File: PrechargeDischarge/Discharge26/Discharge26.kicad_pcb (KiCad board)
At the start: 2 copper layers, 80 x 105 mm, 11 parts, among them J1 HV_Conn, J2 LV_Conn, K4 Relay_SPST-NC, Q1 Q_NMOS_GSD

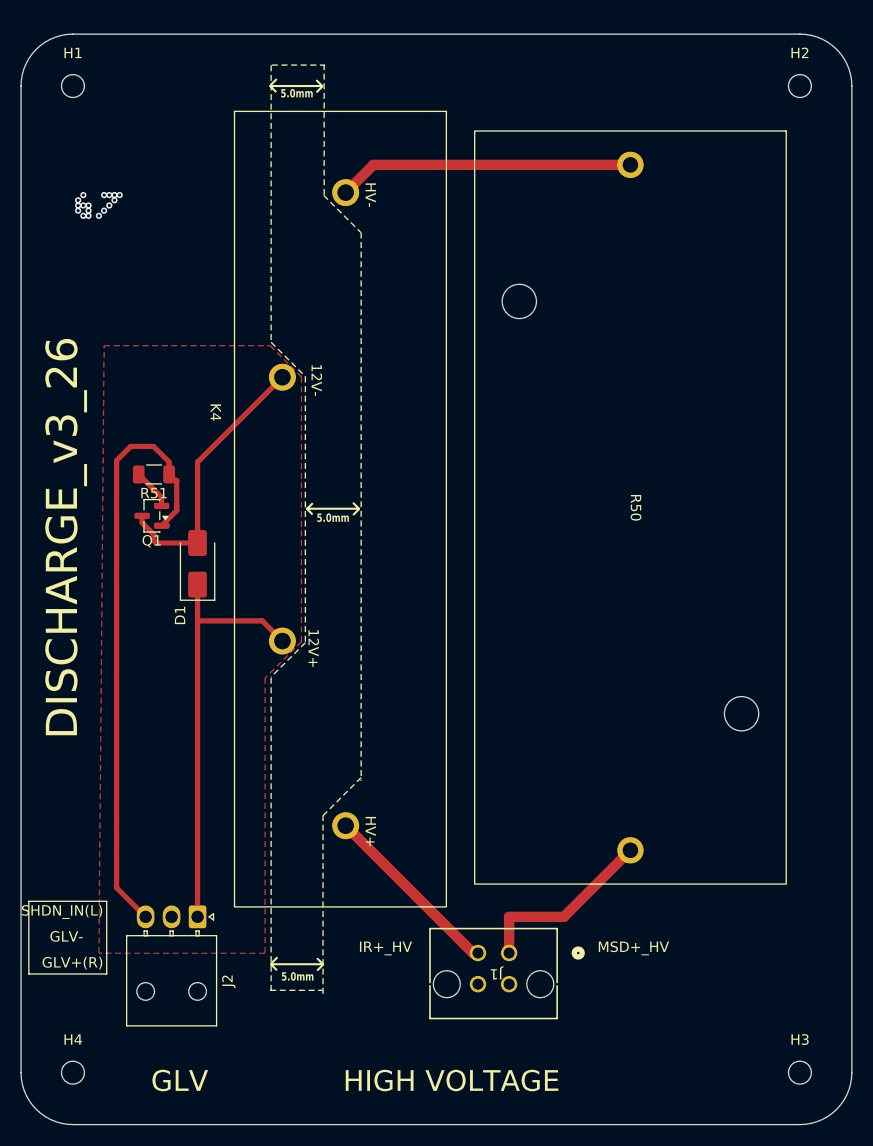
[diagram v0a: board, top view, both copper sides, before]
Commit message: changes mounting holes on discharge to M4
gareth wants all pcb mounting holes to M4
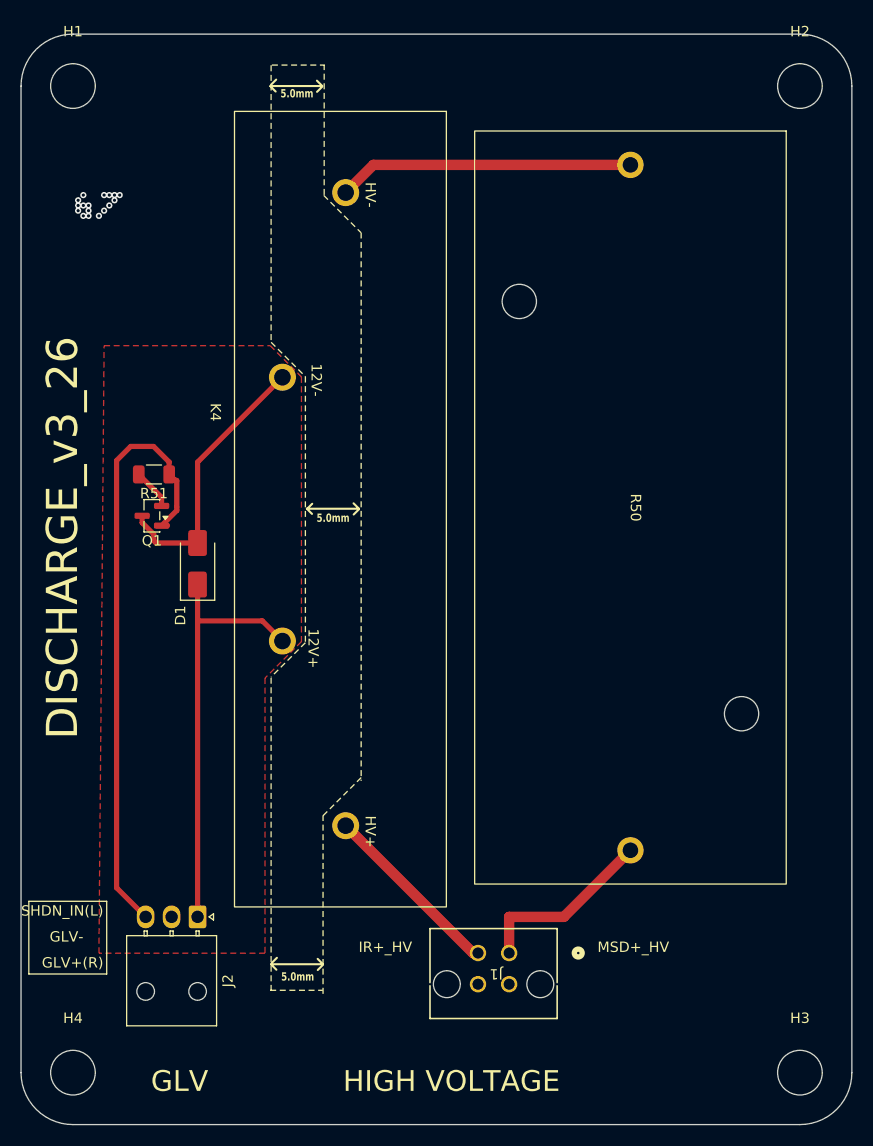
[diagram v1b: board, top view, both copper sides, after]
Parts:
- H1, H2, H3, H4: footprint MountingHole:MountingHole_2.2mm_M2 -> MountingHole:MountingHole_4.3mm_M4
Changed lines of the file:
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@@
 		)
 	)
-	(footprint "MountingHole:MountingHole_2.2mm_M2"
+	(footprint "MountingHole:MountingHole_4.3mm_M4"
 		(layer "F.Cu")
 		(at 130 140)
-		(descr "Mounting Hole 2.2mm, M2, no annular, generated by kicad-footprint-generator mountinghole.py")
-		(tags "mountinghole M2")
+		(descr "Mounting Hole 4.3mm, M4, no annular, generated by kicad-footprint-generator mountinghole.py")
+		(tags "mountinghole M4")
 		(property "Reference" "H4"
-			(at 0 -3.15 0)
+			(at 0 -5.25 0)
 			(layer "F.SilkS")
 			(effects
@@
 		)
 		(property "Value" "MountingHole"
-			(at 0 3.15 0)
+			(at 0 5.25 0)
 			(layer "F.Fab")
 			(effects
@@
 		(fp_circle
 			(center 0 0)
-			(end 2.2 0)
+			(end 4.3 0)
 			(stroke
 				(width 0.15)
@@
 		(fp_circle
 			(center 0 0)
-			(end 2.45 0)
+			(end 4.55 0)
 			(stroke
 				(width 0.05)
@@
 		(pad "" np_thru_hole circle
 			(at 0 0)
-			(size 2.2 2.2)
-			(drill 2.2)
+			(size 4.3 4.3)
+			(drill 4.3)
 			(layers "*.Cu" "*.Mask")
 		)
@@
 		)
 	)
-	(footprint "MountingHole:MountingHole_2.2mm_M2"
+	(footprint "MountingHole:MountingHole_4.3mm_M4"
 		(layer "F.Cu")
 		(at 130 45)
-		(descr "Mounting Hole 2.2mm, M2, no annular, generated by kicad-footprint-generator mountinghole.py")
-		(tags "mountinghole M2")
+		(descr "Mounting Hole 4.3mm, M4, no annular, generated by kicad-footprint-generator mountinghole.py")
+		(tags "mountinghole M4")
 		(property "Reference" "H1"
-			(at 0 -3.15 0)
+			(at 0 -5.25 0)
 			(layer "F.SilkS")
 			(effects
@@
 		)
 		(property "Value" "MountingHole"
-			(at 0 3.15 0)
+			(at 0 5.25 0)
 			(layer "F.Fab")
 			(effects
@@
 		(fp_circle
 			(center 0 0)
-			(end 2.2 0)
+			(end 4.3 0)
 			(stroke
 				(width 0.15)
@@
 		(fp_circle
 			(center 0 0)
-			(end 2.45 0)
+			(end 4.55 0)
 			(stroke
 				(width 0.05)
@@
 		(pad "" np_thru_hole circle
 			(at 0 0)
-			(size 2.2 2.2)
-			(drill 2.2)
+			(size 4.3 4.3)
+			(drill 4.3)
 			(layers "*.Cu" "*.Mask")
 		)
@@
 		(embedded_fonts no)
 	)
-	(footprint "MountingHole:MountingHole_2.2mm_M2"
+	(footprint "MountingHole:MountingHole_4.3mm_M4"
 		(layer "F.Cu")
 		(at 200 140)
-		(descr "Mounting Hole 2.2mm, M2, no annular, generated by kicad-footprint-generator mountinghole.py")
-		(tags "mountinghole M2")
+		(descr "Mounting Hole 4.3mm, M4, no annular, generated by kicad-footprint-generator mountinghole.py")
+		(tags "mountinghole M4")
 		(property "Reference" "H3"
-			(at 0 -3.15 0)
+			(at 0 -5.25 0)
 			(layer "F.SilkS")
 			(effects
@@
 		)
 		(property "Value" "MountingHole"
-			(at 0 3.15 0)
+			(at 0 5.25 0)
 			(layer "F.Fab")
 			(effects
@@
 		(fp_circle
 			(center 0 0)
-			(end 2.2 0)
+			(end 4.3 0)
 			(stroke
 				(width 0.15)
@@
 		(fp_circle
 			(center 0 0)
-			(end 2.45 0)
+			(end 4.55 0)
 			(stroke
 				(width 0.05)
@@
 		(pad "" np_thru_hole circle
 			(at 0 0)
-			(size 2.2 2.2)
-			(drill 2.2)
+			(size 4.3 4.3)
+			(drill 4.3)
 			(layers "*.Cu" "*.Mask")
 		)
@@
 		)
 	)
-	(footprint "MountingHole:MountingHole_2.2mm_M2"
+	(footprint "MountingHole:MountingHole_4.3mm_M4"
 		(layer "F.Cu")
 		(at 200 45)
-		(descr "Mounting Hole 2.2mm, M2, no annular, generated by kicad-footprint-generator mountinghole.py")
-		(tags "mountinghole M2")
+		(descr "Mounting Hole 4.3mm, M4, no annular, generated by kicad-footprint-generator mountinghole.py")
+		(tags "mountinghole M4")
 		(property "Reference" "H2"
-			(at 0 -3.15 0)
+			(at 0 -5.25 0)
 			(layer "F.SilkS")
 			(effects
@@
 		)
 		(property "Value" "MountingHole"
-			(at 0 3.15 0)
+			(at 0 5.25 0)
 			(layer "F.Fab")
 			(effects
@@
 		(fp_circle
 			(center 0 0)
-			(end 2.2 0)
+			(end 4.3 0)
 			(stroke
 				(width 0.15)
@@
 		(fp_circle
 			(center 0 0)
-			(end 2.45 0)
+			(end 4.55 0)
 			(stroke
 				(width 0.05)
@@
 		(pad "" np_thru_hole circle
 			(at 0 0)
-			(size 2.2 2.2)
-			(drill 2.2)
+			(size 4.3 4.3)
+			(drill 4.3)
 			(layers "*.Cu" "*.Mask")
 		)

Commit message: Discharge
Added through hole mosfets and LED driver to DIscharge board
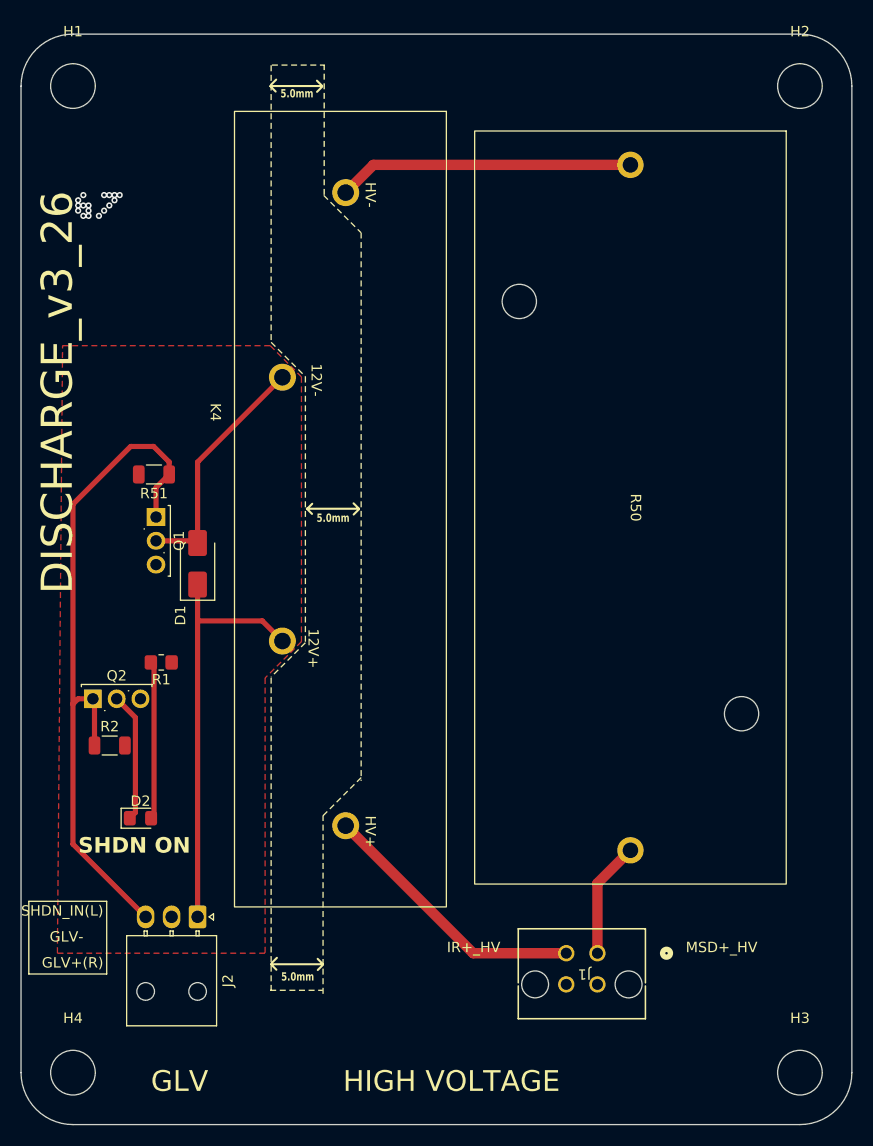
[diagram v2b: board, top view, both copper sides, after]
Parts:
- added D2: LED_DischargeOFF, LED_SMD:LED_0805_2012Metric_Pad1.15x1.40mm_HandSolder, F.Cu at (136.5, 115.5)
- added Q2: Q_NMOS_GDS, Package_TO_SOT_THT:TO-251-3_Vertical, F.Cu at (131.9, 104.0)
- added R1: 2k, Resistor_SMD:R_0805_2012Metric_Pad1.20x1.40mm_HandSolder, F.Cu at (138.5, 100.5)
- added R2: 10k, Resistor_SMD:R_1206_3216Metric, F.Cu at (133.5, 108.5)
- Q1: value Q_NMOS_GSD -> Q_NMOS_GDS; footprint Package_TO_SOT_SMD:SOT-23 -> Package_TO_SOT_THT:TO-251-3_Vertical
- moved J1 8.50 mm to (179.2, 130.0)
- moved Q1 0.42 mm to (138.0, 86.5), turned to -90 degrees
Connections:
- Q1 pad 2: GND -> Net-(D1-A)
- Q1 pad 3: Net-(D1-A) -> GND
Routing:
- net Net-(D2-A): track 0.00 -> 15.2 mm
- net Net-(D2-K): track 0.00 -> 12.5 mm
- net /IR+: track 17.8 -> 26.3 mm
- net /SHDN: track 59.0 -> 67.3 mm
- net /MSD_IN: track 17.8 -> 11.2 mm
- net GND: track 3.94 -> 0.00 mm
- net Net-(D1-A): track 26.5 -> 23.4 mm
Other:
- board text added: "SHDN ON"

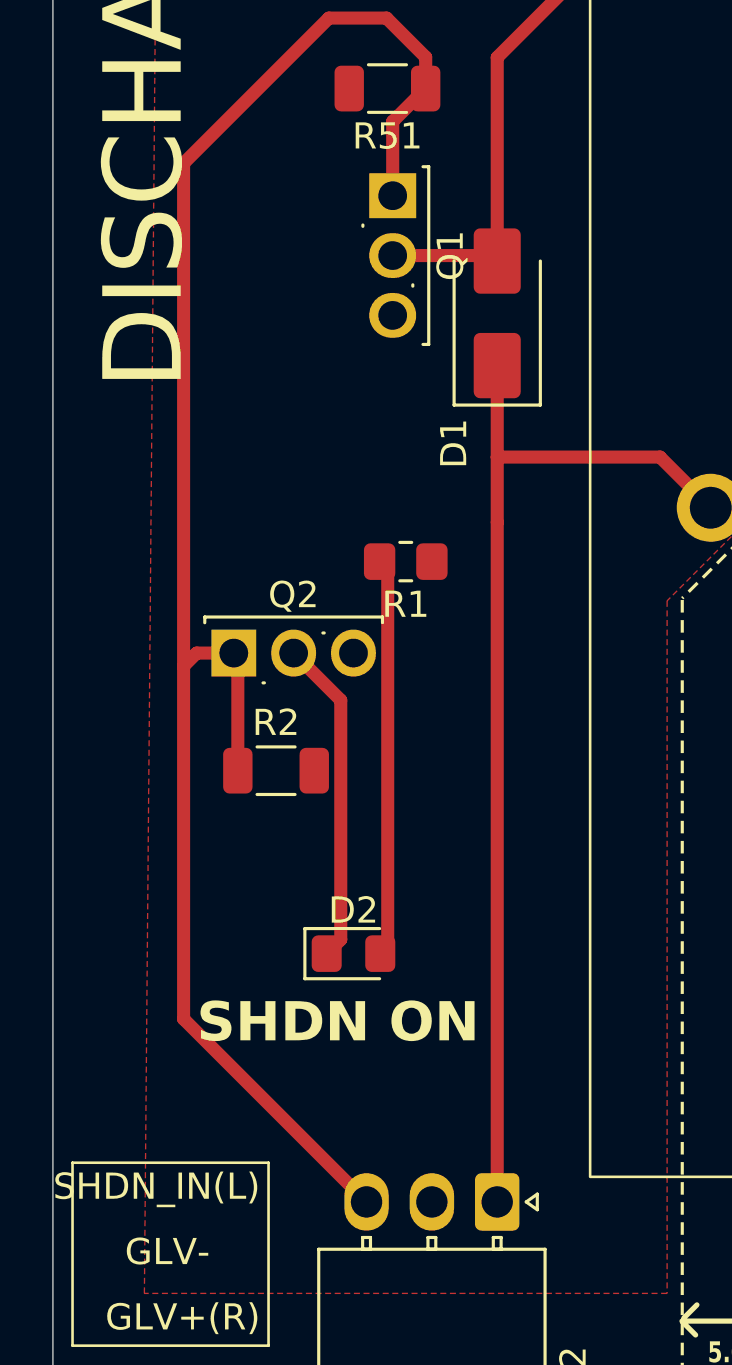
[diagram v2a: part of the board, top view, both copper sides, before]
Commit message: discharge fixed
added zener diode from nmos gate to source, also added indiactor LED
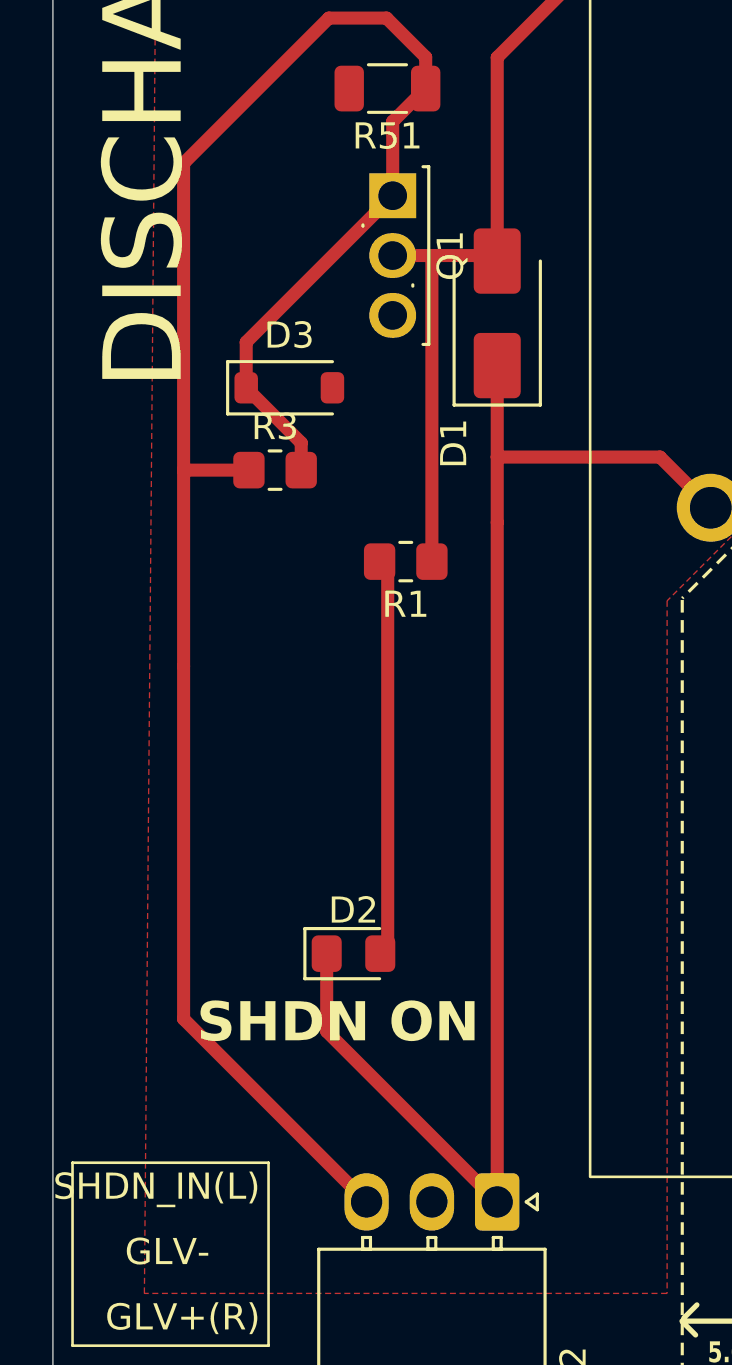
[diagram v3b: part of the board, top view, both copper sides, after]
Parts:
- removed Q2: Q_NMOS_GDS, Package_TO_SOT_THT:TO-251-3_Vertical
- removed R2: 10k, Resistor_SMD:R_1206_3216Metric
- added D3: D_Zener, Diode_SMD:D_SOD-123, F.Cu at (134.0, 93.8)
- added R3: 100, Resistor_SMD:R_0805_2012Metric_Pad1.20x1.40mm_HandSolder, F.Cu at (133.5, 97.0)
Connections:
- D2 pad 1: Net-(D2-K) -> +12V
- Q1 pad 1: /SHDN -> Net-(D3-K)
- R1 pad 1: +12V -> Net-(D1-A)
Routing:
- net Net-(D3-K): track 0.00 -> 13.0 mm
- net Net-(D2-K): track 12.5 -> 0.00 mm
- net +12V: track 41.0 -> 53.2 mm
- net Net-(D1-A): track 23.4 -> 35.1 mm
- net /SHDN: track 67.3 -> 63.1 mm

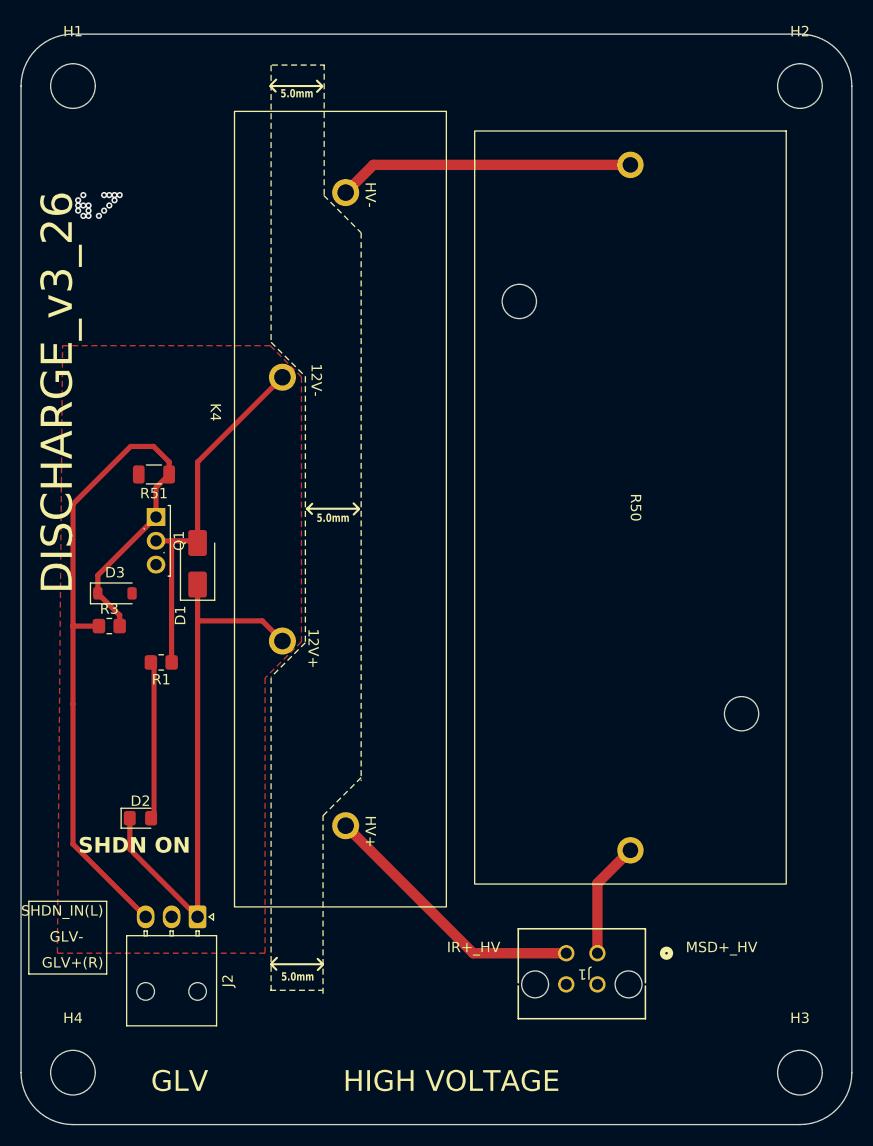
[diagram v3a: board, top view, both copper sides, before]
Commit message: Fixed Discharge + Added RML Quick files
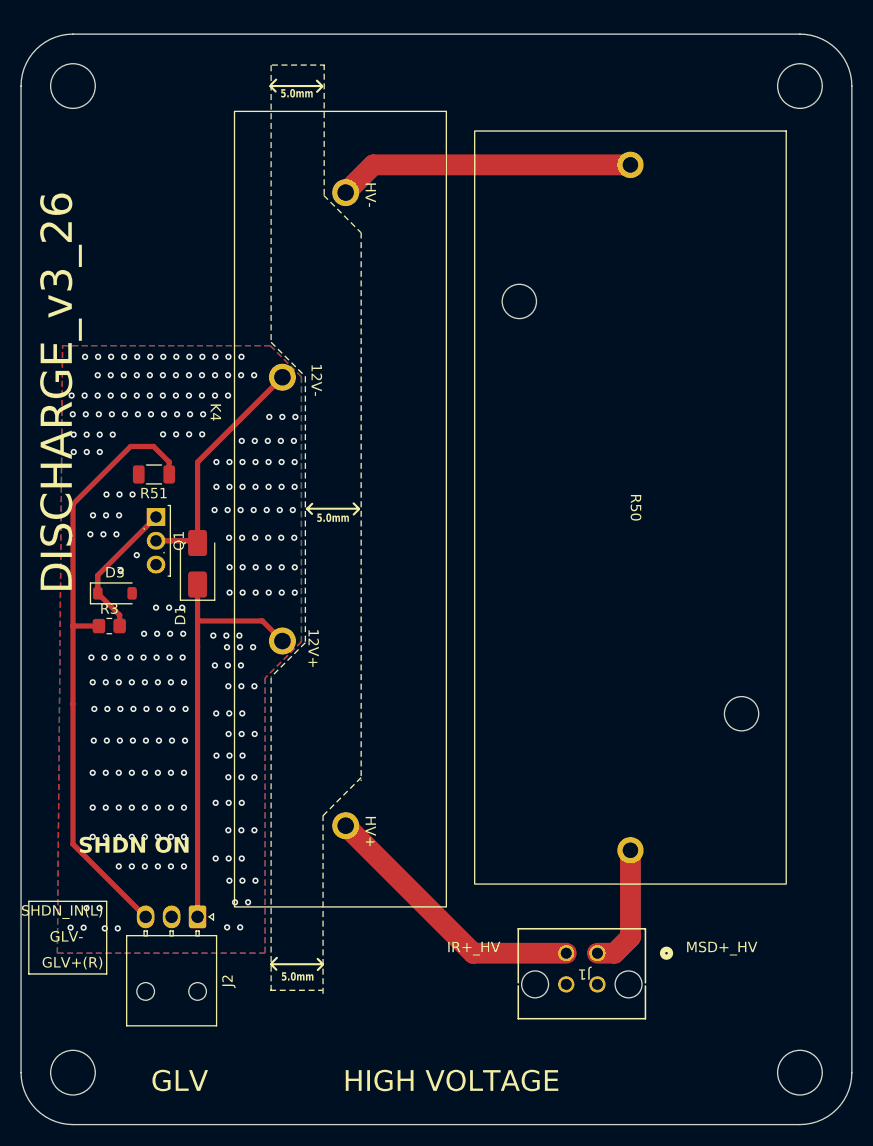
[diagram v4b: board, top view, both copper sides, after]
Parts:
- removed D2: LED_DischargeOFF, LED_SMD:LED_0805_2012Metric_Pad1.15x1.40mm_HandSolder
- removed R1: 2k, Resistor_SMD:R_0805_2012Metric_Pad1.20x1.40mm_HandSolder
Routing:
- net Net-(D2-A): track 15.2 -> 0.00 mm
- net +12V: track 53.2 -> 41.0 mm
- net Net-(D1-A): track 35.1 -> 23.4 mm
- net /SHDN: track 63.1 -> 58.5 mm
- net /MSD_IN: track 11.2 -> 12.2 mm
- net GND: vias 0 -> 234
- net (no net): vias 17 -> 0
- added copper zone on B.Cu, net GND
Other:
- board text added: "12V-"
- board text added: "K1"
